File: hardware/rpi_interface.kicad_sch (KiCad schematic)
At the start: 5 parts, among them J14 RPI_Connector, M1 Noctua NF-A4x10

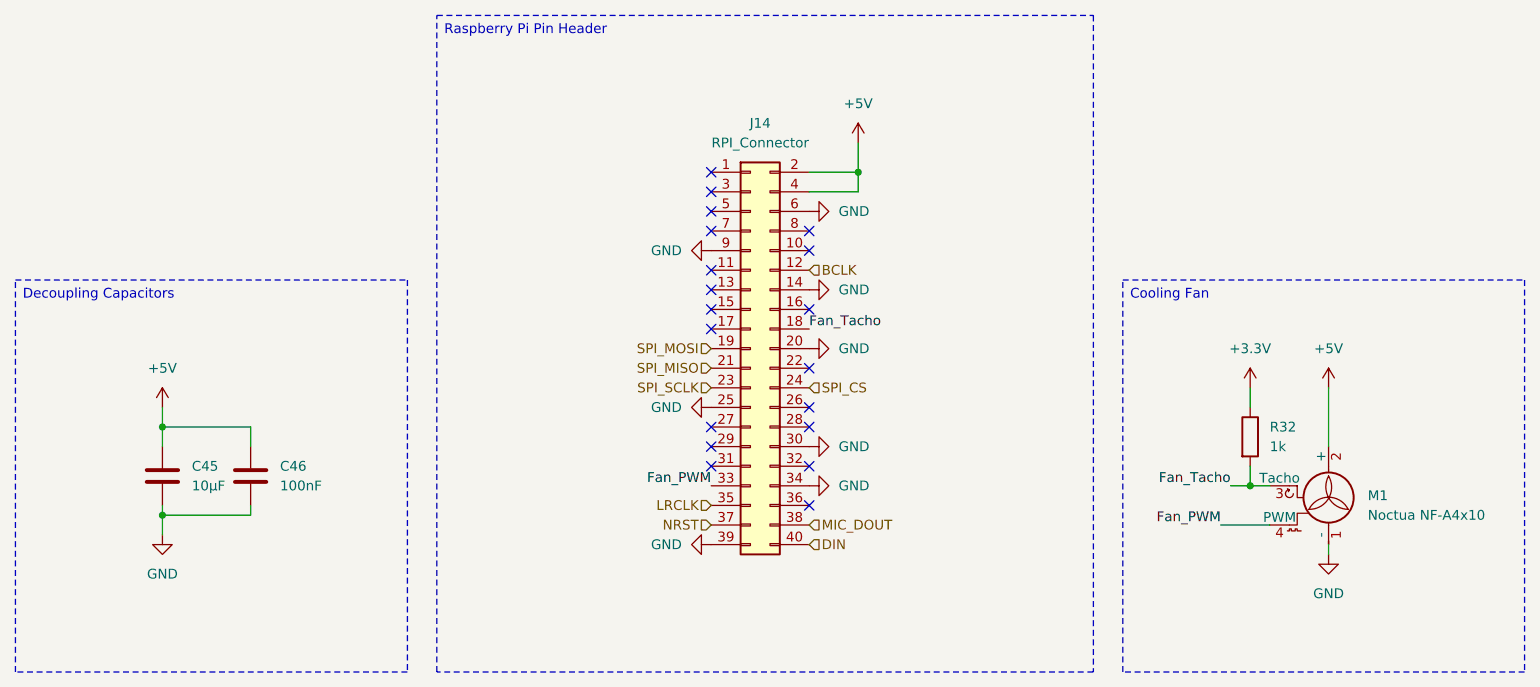
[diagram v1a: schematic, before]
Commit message: IMU modification and Power monitor addition
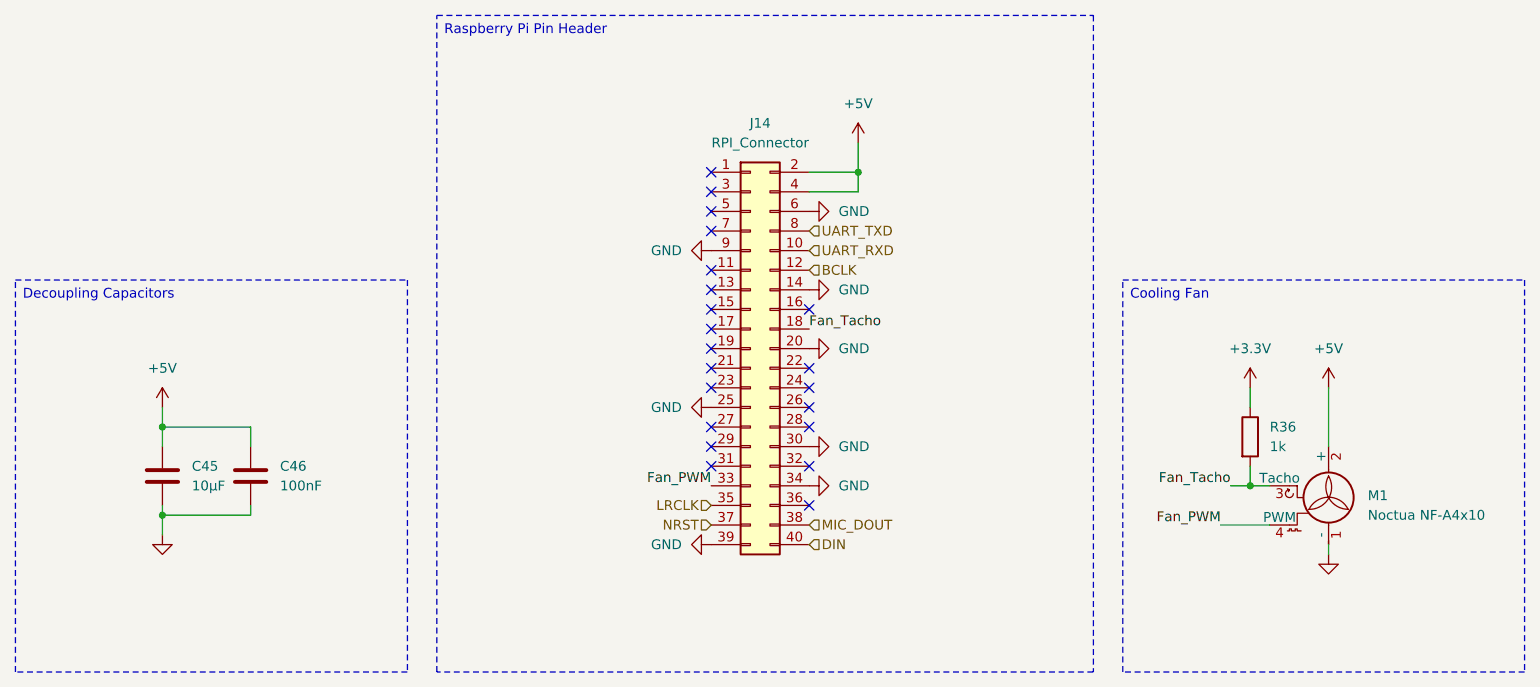
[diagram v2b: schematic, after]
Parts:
- renumbered R32 to R36
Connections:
- net UART_RXD: now reaches J14.10 (Pin_10)
- net UART_TXD: now reaches J14.8 (Pin_8)
- net SPI_CS: no longer names the net of J14.24 (Pin_24)
- net SPI_MISO: no longer names the net of J14.21 (Pin_21)
- net SPI_MOSI: no longer names the net of J14.19 (Pin_19)
- net SPI_SCLK: no longer names the net of J14.23 (Pin_23)
- no-connect marks 19 -> 21
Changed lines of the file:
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@@
 	)
 	(no_connect
-		(at 154.94 85.09)
-	)
-	(no_connect
 		(at 142.24 90.17)
 	)
@@
 	)
 	(no_connect
+		(at 154.94 105.41)
+	)
+	(no_connect
 		(at 154.94 95.25)
 	)
 	(no_connect
+		(at 142.24 100.33)
+	)
+	(no_connect
 		(at 154.94 110.49)
 	)
 	(no_connect
-		(at 142.24 92.71)
+		(at 142.24 105.41)
 	)
 	(no_connect
-		(at 154.94 87.63)
+		(at 142.24 92.71)
 	)
 	(no_connect
@@
 	)
 	(no_connect
+		(at 142.24 102.87)
+	)
+	(no_connect
 		(at 154.94 120.65)
 	)
@@
 		)
 	)
-	(hierarchical_label "SPI_CS"
+	(hierarchical_label "MIC_DOUT"
 		(shape input)
-		(at 154.94 105.41 0)
+		(at 154.94 123.19 0)
 		(effects
 			(font
@@
 		)
 	)
-	(hierarchical_label "MIC_DOUT"
+	(hierarchical_label "UART_RXD"
 		(shape input)
-		(at 154.94 123.19 0)
+		(at 154.94 87.63 0)
 		(effects
 			(font
@@
 		)
 	)
-	(hierarchical_label "SPI_MOSI"
-		(shape input)
-		(at 142.24 100.33 180)
-		(effects
-			(font
-				(size 1.27 1.27)
-			)
-			(justify right)
-		)
-	)
 	(hierarchical_label "BCLK"
 		(shape input)
@@
 		)
 	)
-	(hierarchical_label "SPI_SCLK"
-		(shape input)
-		(at 142.24 105.41 180)
-		(effects
-			(font
-				(size 1.27 1.27)
-			)
-			(justify right)
-		)
-	)
-	(hierarchical_label "SPI_MISO"
+	(hierarchical_label "UART_TXD"
 		(shape input)
-		(at 142.24 102.87 180)
+		(at 154.94 85.09 0)
 		(effects
 			(font
 				(size 1.27 1.27)
 			)
-			(justify right)
+			(justify left)
 		)
 	)
@@
 		(dnp no)
 		(fields_autoplaced yes)
-		(property "Reference" "#PWR0102"
+		(property "Reference" "#PWR0106"
 			(at 161.29 92.71 0)
 			(effects
@@
 			(project "chromapi_motherboard_v1"
 				(path "/d1a31f26-03e0-43e1-89c1-031fe31befc5/e996aba6-741c-4e73-a7c7-e6548b7ec52f"
-					(reference "#PWR0102")
+					(reference "#PWR0106")
 					(unit 1)
 				)
@@
 		(dnp no)
 		(fields_autoplaced yes)
-		(property "Reference" "#PWR0112"
+		(property "Reference" "#PWR0116"
 			(at 222.25 133.35 0)
 			(effects
@@
 					(size 1.27 1.27)
 				)
+				(hide yes)
 			)
 		)
@@
 			(project "chromapi_motherboard_v1"
 				(path "/d1a31f26-03e0-43e1-89c1-031fe31befc5/e996aba6-741c-4e73-a7c7-e6548b7ec52f"
-					(reference "#PWR0112")
+					(reference "#PWR0116")
 					(unit 1)
 				)
@@
 		(dnp no)
 		(fields_autoplaced yes)
-		(property "Reference" "#PWR0110"
+		(property "Reference" "#PWR0114"
 			(at 71.12 130.81 0)
 			(effects
@@
 					(size 1.27 1.27)
 				)
+				(hide yes)
 			)
 		)
@@
 			(project ""
 				(path "/d1a31f26-03e0-43e1-89c1-031fe31befc5/e996aba6-741c-4e73-a7c7-e6548b7ec52f"
-					(reference "#PWR0110")
+					(reference "#PWR0114")
 					(unit 1)
 				)
@@
 		(dnp no)
 		(fields_autoplaced yes)
-		(property "Reference" "#PWR0101"
+		(property "Reference" "#PWR0105"
 			(at 135.89 87.63 0)
 			(effects
@@
 			(project "chromapi_motherboard_v1"
 				(path "/d1a31f26-03e0-43e1-89c1-031fe31befc5/e996aba6-741c-4e73-a7c7-e6548b7ec52f"
-					(reference "#PWR0101")
+					(reference "#PWR0105")
 					(unit 1)
 				)
@@
 		(dnp no)
 		(fields_autoplaced yes)
-		(property "Reference" "R32"
+		(property "Reference" "R36"
 			(at 214.63 110.4899 0)
 			(effects
@@
 			(project ""
 				(path "/d1a31f26-03e0-43e1-89c1-031fe31befc5/e996aba6-741c-4e73-a7c7-e6548b7ec52f"
-					(reference "R32")
+					(reference "R36")
 					(unit 1)
 				)
@@
 		(on_board yes)
 		(dnp no)
-		(property "Reference" "#PWR0106"
+		(property "Reference" "#PWR0110"
 			(at 71.12 111.76 0)
 			(effects
@@
 			(project ""
 				(path "/d1a31f26-03e0-43e1-89c1-031fe31befc5/e996aba6-741c-4e73-a7c7-e6548b7ec52f"
-					(reference "#PWR0106")
+					(reference "#PWR0110")
 					(unit 1)
 				)
@@
 		(dnp no)
 		(fields_autoplaced yes)
-		(property "Reference" "#PWR0111"
+		(property "Reference" "#PWR0115"
 			(at 135.89 125.73 0)
 			(effects
@@
 			(project "chromapi_motherboard_v1"
 				(path "/d1a31f26-03e0-43e1-89c1-031fe31befc5/e996aba6-741c-4e73-a7c7-e6548b7ec52f"
-					(reference "#PWR0111")
+					(reference "#PWR0115")
 					(unit 1)
 				)
@@
 		(dnp no)
 		(fields_autoplaced yes)
-		(property "Reference" "#PWR099"
+		(property "Reference" "#PWR0103"
 			(at 161.29 77.47 0)
 			(effects
@@
 			(project ""
 				(path "/d1a31f26-03e0-43e1-89c1-031fe31befc5/e996aba6-741c-4e73-a7c7-e6548b7ec52f"
-					(reference "#PWR099")
+					(reference "#PWR0103")
 					(unit 1)
 				)
@@
 		(dnp no)
 		(fields_autoplaced yes)
-		(property "Reference" "#PWR0100"
+		(property "Reference" "#PWR0104"
 			(at 161.29 82.55 0)
 			(effects
@@
 			(project "chromapi_motherboard_v1"
 				(path "/d1a31f26-03e0-43e1-89c1-031fe31befc5/e996aba6-741c-4e73-a7c7-e6548b7ec52f"
-					(reference "#PWR0100")
+					(reference "#PWR0104")
 					(unit 1)
 				)
@@
 		(dnp no)
 		(fields_autoplaced yes)
-		(property "Reference" "#PWR0109"
+		(property "Reference" "#PWR0113"
 			(at 161.29 118.11 0)
 			(effects
@@
 			(project "chromapi_motherboard_v1"
 				(path "/d1a31f26-03e0-43e1-89c1-031fe31befc5/e996aba6-741c-4e73-a7c7-e6548b7ec52f"
-					(reference "#PWR0109")
+					(reference "#PWR0113")
 					(unit 1)
 				)
@@
 		(dnp no)
 		(fields_autoplaced yes)
-		(property "Reference" "#PWR0108"
+		(property "Reference" "#PWR0112"
 			(at 161.29 113.03 0)
 			(effects
@@
 			(project "chromapi_motherboard_v1"
 				(path "/d1a31f26-03e0-43e1-89c1-031fe31befc5/e996aba6-741c-4e73-a7c7-e6548b7ec52f"
-					(reference "#PWR0108")
+					(reference "#PWR0112")
 					(unit 1)
 				)
@@
 		(dnp no)
 		(fields_autoplaced yes)
-		(property "Reference" "#PWR0105"
+		(property "Reference" "#PWR0109"
 			(at 222.25 109.22 0)
 			(effects
@@
 			(project "chromapi_motherboard_v1"
 				(path "/d1a31f26-03e0-43e1-89c1-031fe31befc5/e996aba6-741c-4e73-a7c7-e6548b7ec52f"
-					(reference "#PWR0105")
+					(reference "#PWR0109")
 					(unit 1)
 				)
@@
 		(dnp no)
 		(fields_autoplaced yes)
-		(property "Reference" "#PWR0103"
+		(property "Reference" "#PWR0107"
 			(at 161.29 100.33 0)
 			(effects
@@
 			(project "chromapi_motherboard_v1"
 				(path "/d1a31f26-03e0-43e1-89c1-031fe31befc5/e996aba6-741c-4e73-a7c7-e6548b7ec52f"
-					(reference "#PWR0103")
+					(reference "#PWR0107")
 					(unit 1)
 				)
@@
 		(dnp no)
 		(fields_autoplaced yes)
-		(property "Reference" "#PWR0104"
+		(property "Reference" "#PWR0108"
 			(at 212.09 109.22 0)
 			(effects
@@
 			(project ""
 				(path "/d1a31f26-03e0-43e1-89c1-031fe31befc5/e996aba6-741c-4e73-a7c7-e6548b7ec52f"
-					(reference "#PWR0104")
+					(reference "#PWR0108")
 					(unit 1)
 				)
@@
 		(dnp no)
 		(fields_autoplaced yes)
-		(property "Reference" "#PWR0107"
+		(property "Reference" "#PWR0111"
 			(at 135.89 107.95 0)
 			(effects
@@
 			(project "chromapi_motherboard_v1"
 				(path "/d1a31f26-03e0-43e1-89c1-031fe31befc5/e996aba6-741c-4e73-a7c7-e6548b7ec52f"
-					(reference "#PWR0107")
+					(reference "#PWR0111")
 					(unit 1)
 				)

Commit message: Upgrading voltage regulation circuit in schematic
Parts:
- renumbered C45 to C42, C46 to C43
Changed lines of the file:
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@@
 		(dnp no)
 		(fields_autoplaced yes)
-		(property "Reference" "#PWR0106"
+		(property "Reference" "#PWR0104"
 			(at 161.29 92.71 0)
 			(effects
@@
 			(project "chromapi_motherboard_v1"
 				(path "/d1a31f26-03e0-43e1-89c1-031fe31befc5/e996aba6-741c-4e73-a7c7-e6548b7ec52f"
-					(reference "#PWR0106")
+					(reference "#PWR0104")
 					(unit 1)
 				)
@@
 		(dnp no)
 		(fields_autoplaced yes)
-		(property "Reference" "C46"
+		(property "Reference" "C43"
 			(at 86.36 115.5699 0)
 			(effects
@@
 			(project ""
 				(path "/d1a31f26-03e0-43e1-89c1-031fe31befc5/e996aba6-741c-4e73-a7c7-e6548b7ec52f"
-					(reference "C46")
+					(reference "C43")
 					(unit 1)
 				)
@@
 		(dnp no)
 		(fields_autoplaced yes)
-		(property "Reference" "#PWR0116"
+		(property "Reference" "#PWR0114"
 			(at 222.25 133.35 0)
 			(effects
@@
 			(project "chromapi_motherboard_v1"
 				(path "/d1a31f26-03e0-43e1-89c1-031fe31befc5/e996aba6-741c-4e73-a7c7-e6548b7ec52f"
-					(reference "#PWR0116")
+					(reference "#PWR0114")
 					(unit 1)
 				)
@@
 		(dnp no)
 		(fields_autoplaced yes)
-		(property "Reference" "#PWR0114"
+		(property "Reference" "#PWR0112"
 			(at 71.12 130.81 0)
 			(effects
@@
 			(project ""
 				(path "/d1a31f26-03e0-43e1-89c1-031fe31befc5/e996aba6-741c-4e73-a7c7-e6548b7ec52f"
-					(reference "#PWR0114")
+					(reference "#PWR0112")
 					(unit 1)
 				)
@@
 		(dnp no)
 		(fields_autoplaced yes)
-		(property "Reference" "#PWR0105"
+		(property "Reference" "#PWR0103"
 			(at 135.89 87.63 0)
 			(effects
@@
 			(project "chromapi_motherboard_v1"
 				(path "/d1a31f26-03e0-43e1-89c1-031fe31befc5/e996aba6-741c-4e73-a7c7-e6548b7ec52f"
-					(reference "#PWR0105")
+					(reference "#PWR0103")
 					(unit 1)
 				)
@@
 		(on_board yes)
 		(dnp no)
-		(property "Reference" "#PWR0110"
+		(property "Reference" "#PWR0108"
 			(at 71.12 111.76 0)
 			(effects
@@
 			(project ""
 				(path "/d1a31f26-03e0-43e1-89c1-031fe31befc5/e996aba6-741c-4e73-a7c7-e6548b7ec52f"
-					(reference "#PWR0110")
+					(reference "#PWR0108")
 					(unit 1)
 				)
@@
 		(dnp no)
 		(fields_autoplaced yes)
-		(property "Reference" "#PWR0115"
+		(property "Reference" "#PWR0113"
 			(at 135.89 125.73 0)
 			(effects
@@
 			(project "chromapi_motherboard_v1"
 				(path "/d1a31f26-03e0-43e1-89c1-031fe31befc5/e996aba6-741c-4e73-a7c7-e6548b7ec52f"
-					(reference "#PWR0115")
+					(reference "#PWR0113")
 					(unit 1)
 				)
@@
 		(dnp no)
 		(fields_autoplaced yes)
-		(property "Reference" "#PWR0103"
+		(property "Reference" "#PWR0101"
 			(at 161.29 77.47 0)
 			(effects
@@
 			(project ""
 				(path "/d1a31f26-03e0-43e1-89c1-031fe31befc5/e996aba6-741c-4e73-a7c7-e6548b7ec52f"
-					(reference "#PWR0103")
+					(reference "#PWR0101")
 					(unit 1)
 				)
@@
 		(dnp no)
 		(fields_autoplaced yes)
-		(property "Reference" "#PWR0104"
+		(property "Reference" "#PWR0102"
 			(at 161.29 82.55 0)
 			(effects
@@
 			(project "chromapi_motherboard_v1"
 				(path "/d1a31f26-03e0-43e1-89c1-031fe31befc5/e996aba6-741c-4e73-a7c7-e6548b7ec52f"
-					(reference "#PWR0104")
+					(reference "#PWR0102")
 					(unit 1)
 				)
@@
 		(dnp no)
 		(fields_autoplaced yes)
-		(property "Reference" "#PWR0113"
+		(property "Reference" "#PWR0111"
 			(at 161.29 118.11 0)
 			(effects
@@
 			(project "chromapi_motherboard_v1"
 				(path "/d1a31f26-03e0-43e1-89c1-031fe31befc5/e996aba6-741c-4e73-a7c7-e6548b7ec52f"
-					(reference "#PWR0113")
+					(reference "#PWR0111")
 					(unit 1)
 				)
@@
 		(dnp no)
 		(fields_autoplaced yes)
-		(property "Reference" "#PWR0112"
+		(property "Reference" "#PWR0110"
 			(at 161.29 113.03 0)
 			(effects
@@
 			(project "chromapi_motherboard_v1"
 				(path "/d1a31f26-03e0-43e1-89c1-031fe31befc5/e996aba6-741c-4e73-a7c7-e6548b7ec52f"
-					(reference "#PWR0112")
+					(reference "#PWR0110")
 					(unit 1)
 				)
@@
 		(dnp no)
 		(fields_autoplaced yes)
-		(property "Reference" "#PWR0109"
+		(property "Reference" "#PWR0107"
 			(at 222.25 109.22 0)
 			(effects
@@
 			(project "chromapi_motherboard_v1"
 				(path "/d1a31f26-03e0-43e1-89c1-031fe31befc5/e996aba6-741c-4e73-a7c7-e6548b7ec52f"
-					(reference "#PWR0109")
+					(reference "#PWR0107")
 					(unit 1)
 				)
@@
 		(dnp no)
 		(fields_autoplaced yes)
-		(property "Reference" "#PWR0107"
+		(property "Reference" "#PWR0105"
 			(at 161.29 100.33 0)
 			(effects
@@
 			(project "chromapi_motherboard_v1"
 				(path "/d1a31f26-03e0-43e1-89c1-031fe31befc5/e996aba6-741c-4e73-a7c7-e6548b7ec52f"
-					(reference "#PWR0107")
+					(reference "#PWR0105")
 					(unit 1)
 				)
@@
 		(dnp no)
 		(fields_autoplaced yes)
-		(property "Reference" "#PWR0108"
+		(property "Reference" "#PWR0106"
 			(at 212.09 109.22 0)
 			(effects
@@
 			(project ""
 				(path "/d1a31f26-03e0-43e1-89c1-031fe31befc5/e996aba6-741c-4e73-a7c7-e6548b7ec52f"
-					(reference "#PWR0108")
+					(reference "#PWR0106")
 					(unit 1)
 				)
@@
 		(dnp no)
 		(fields_autoplaced yes)
-		(property "Reference" "#PWR0111"
+		(property "Reference" "#PWR0109"
 			(at 135.89 107.95 0)
 			(effects
@@
 			(project "chromapi_motherboard_v1"
 				(path "/d1a31f26-03e0-43e1-89c1-031fe31befc5/e996aba6-741c-4e73-a7c7-e6548b7ec52f"
-					(reference "#PWR0111")
+					(reference "#PWR0109")
 					(unit 1)
 				)
@@
 		(dnp no)
 		(fields_autoplaced yes)
-		(property "Reference" "C45"
+		(property "Reference" "C42"
 			(at 74.93 115.5699 0)
 			(effects
@@
 			(project "chromapi_motherboard_v1"
 				(path "/d1a31f26-03e0-43e1-89c1-031fe31befc5/e996aba6-741c-4e73-a7c7-e6548b7ec52f"
-					(reference "C45")
-					(unit 1)
-				)
+					(reference "C42")
+					(unit 1)
+				)

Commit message: Running ERC successfully
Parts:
- renumbered R36 to R37
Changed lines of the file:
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@@
 		(dnp no)
 		(fields_autoplaced yes)
-		(property "Reference" "#PWR0104"
+		(property "Reference" "#PWR0105"
 			(at 161.29 92.71 0)
 			(effects
@@
 			(project "chromapi_motherboard_v1"
 				(path "/d1a31f26-03e0-43e1-89c1-031fe31befc5/e996aba6-741c-4e73-a7c7-e6548b7ec52f"
-					(reference "#PWR0104")
+					(reference "#PWR0105")
 					(unit 1)
 				)
@@
 		(dnp no)
 		(fields_autoplaced yes)
-		(property "Reference" "#PWR0114"
+		(property "Reference" "#PWR0115"
 			(at 222.25 133.35 0)
 			(effects
@@
 			(project "chromapi_motherboard_v1"
 				(path "/d1a31f26-03e0-43e1-89c1-031fe31befc5/e996aba6-741c-4e73-a7c7-e6548b7ec52f"
-					(reference "#PWR0114")
+					(reference "#PWR0115")
 					(unit 1)
 				)
@@
 		(dnp no)
 		(fields_autoplaced yes)
-		(property "Reference" "#PWR0112"
+		(property "Reference" "#PWR0113"
 			(at 71.12 130.81 0)
 			(effects
@@
 			(project ""
 				(path "/d1a31f26-03e0-43e1-89c1-031fe31befc5/e996aba6-741c-4e73-a7c7-e6548b7ec52f"
-					(reference "#PWR0112")
+					(reference "#PWR0113")
 					(unit 1)
 				)
@@
 		(dnp no)
 		(fields_autoplaced yes)
-		(property "Reference" "#PWR0103"
+		(property "Reference" "#PWR0104"
 			(at 135.89 87.63 0)
 			(effects
@@
 			(project "chromapi_motherboard_v1"
 				(path "/d1a31f26-03e0-43e1-89c1-031fe31befc5/e996aba6-741c-4e73-a7c7-e6548b7ec52f"
-					(reference "#PWR0103")
+					(reference "#PWR0104")
 					(unit 1)
 				)
@@
 		(dnp no)
 		(fields_autoplaced yes)
-		(property "Reference" "R36"
+		(property "Reference" "R37"
 			(at 214.63 110.4899 0)
 			(effects
@@
 			(project ""
 				(path "/d1a31f26-03e0-43e1-89c1-031fe31befc5/e996aba6-741c-4e73-a7c7-e6548b7ec52f"
-					(reference "R36")
+					(reference "R37")
 					(unit 1)
 				)
@@
 		(on_board yes)
 		(dnp no)
-		(property "Reference" "#PWR0108"
+		(property "Reference" "#PWR0109"
 			(at 71.12 111.76 0)
 			(effects
@@
 			(project ""
 				(path "/d1a31f26-03e0-43e1-89c1-031fe31befc5/e996aba6-741c-4e73-a7c7-e6548b7ec52f"
-					(reference "#PWR0108")
+					(reference "#PWR0109")
 					(unit 1)
 				)
@@
 		(dnp no)
 		(fields_autoplaced yes)
-		(property "Reference" "#PWR0113"
+		(property "Reference" "#PWR0114"
 			(at 135.89 125.73 0)
 			(effects
@@
 			(project "chromapi_motherboard_v1"
 				(path "/d1a31f26-03e0-43e1-89c1-031fe31befc5/e996aba6-741c-4e73-a7c7-e6548b7ec52f"
-					(reference "#PWR0113")
+					(reference "#PWR0114")
 					(unit 1)
 				)
@@
 		(dnp no)
 		(fields_autoplaced yes)
-		(property "Reference" "#PWR0101"
+		(property "Reference" "#PWR0102"
 			(at 161.29 77.47 0)
 			(effects
@@
 			(project ""
 				(path "/d1a31f26-03e0-43e1-89c1-031fe31befc5/e996aba6-741c-4e73-a7c7-e6548b7ec52f"
-					(reference "#PWR0101")
+					(reference "#PWR0102")
 					(unit 1)
 				)
@@
 		(dnp no)
 		(fields_autoplaced yes)
-		(property "Reference" "#PWR0102"
+		(property "Reference" "#PWR0103"
 			(at 161.29 82.55 0)
 			(effects
@@
 			(project "chromapi_motherboard_v1"
 				(path "/d1a31f26-03e0-43e1-89c1-031fe31befc5/e996aba6-741c-4e73-a7c7-e6548b7ec52f"
-					(reference "#PWR0102")
+					(reference "#PWR0103")
 					(unit 1)
 				)
@@
 		(dnp no)
 		(fields_autoplaced yes)
-		(property "Reference" "#PWR0111"
+		(property "Reference" "#PWR0112"
 			(at 161.29 118.11 0)
 			(effects
@@
 			(project "chromapi_motherboard_v1"
 				(path "/d1a31f26-03e0-43e1-89c1-031fe31befc5/e996aba6-741c-4e73-a7c7-e6548b7ec52f"
-					(reference "#PWR0111")
+					(reference "#PWR0112")
 					(unit 1)
 				)
@@
 		(dnp no)
 		(fields_autoplaced yes)
-		(property "Reference" "#PWR0110"
+		(property "Reference" "#PWR0111"
 			(at 161.29 113.03 0)
 			(effects
@@
 			(project "chromapi_motherboard_v1"
 				(path "/d1a31f26-03e0-43e1-89c1-031fe31befc5/e996aba6-741c-4e73-a7c7-e6548b7ec52f"
-					(reference "#PWR0110")
+					(reference "#PWR0111")
 					(unit 1)
 				)
@@
 		(dnp no)
 		(fields_autoplaced yes)
-		(property "Reference" "#PWR0107"
+		(property "Reference" "#PWR0108"
 			(at 222.25 109.22 0)
 			(effects
@@
 			(project "chromapi_motherboard_v1"
 				(path "/d1a31f26-03e0-43e1-89c1-031fe31befc5/e996aba6-741c-4e73-a7c7-e6548b7ec52f"
-					(reference "#PWR0107")
+					(reference "#PWR0108")
 					(unit 1)
 				)
@@
 		(dnp no)
 		(fields_autoplaced yes)
-		(property "Reference" "#PWR0105"
+		(property "Reference" "#PWR0106"
 			(at 161.29 100.33 0)
 			(effects
@@
 			(project "chromapi_motherboard_v1"
 				(path "/d1a31f26-03e0-43e1-89c1-031fe31befc5/e996aba6-741c-4e73-a7c7-e6548b7ec52f"
-					(reference "#PWR0105")
+					(reference "#PWR0106")
 					(unit 1)
 				)
@@
 		(dnp no)
 		(fields_autoplaced yes)
-		(property "Reference" "#PWR0106"
+		(property "Reference" "#PWR0107"
 			(at 212.09 109.22 0)
 			(effects
@@
 			(project ""
 				(path "/d1a31f26-03e0-43e1-89c1-031fe31befc5/e996aba6-741c-4e73-a7c7-e6548b7ec52f"
-					(reference "#PWR0106")
+					(reference "#PWR0107")
 					(unit 1)
 				)
@@
 		(dnp no)
 		(fields_autoplaced yes)
-		(property "Reference" "#PWR0109"
+		(property "Reference" "#PWR0110"
 			(at 135.89 107.95 0)
 			(effects
@@
 			(project "chromapi_motherboard_v1"
 				(path "/d1a31f26-03e0-43e1-89c1-031fe31befc5/e996aba6-741c-4e73-a7c7-e6548b7ec52f"
-					(reference "#PWR0109")
-					(unit 1)
-				)
+					(reference "#PWR0110")
+					(unit 1)
+				)
